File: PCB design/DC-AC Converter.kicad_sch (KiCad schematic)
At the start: 19 parts, among them J1 Screw_Terminal_3.5mm_2, J2 Conn_02x02_Counter_Clockwise, J3 Screw_Terminal_3.5mm_2, J4 Conn_01x02, Q1 IRF9540N, Q2 IRFZ44NSTRLPBF, Q3 IRF9540N, Q4 IRFZ44NSTRLPBF, U1 ATtiny85V-10P, U3 L78L05_SOT89

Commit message: some SMD components changed to PTH footprint
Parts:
- Q1, Q2, Q4: footprint Package_TO_SOT_SMD:TO-263-2 -> Package_TO_SOT_THT:TO-264-3_Horizontal_TabDown
- U1: footprint Package_SO:SOP-8_5.28x5.23mm_P1.27mm -> Package_DIP:DIP-8_W7.62mm_Socket
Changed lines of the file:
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@@
 		)
 		(instances
-			(project "AC_M V2"
+			(project "DC-AC Converter"
 				(path "/907d77e3-c168-455a-b3e6-ab5b57505f53"
 					(reference "FID1")
@@
 		)
 		(instances
-			(project "AC_M V2"
+			(project "DC-AC Converter"
 				(path "/907d77e3-c168-455a-b3e6-ab5b57505f53"
 					(reference "H4")
@@
 		)
 		(instances
-			(project "AC_M V2"
+			(project "DC-AC Converter"
 				(path "/907d77e3-c168-455a-b3e6-ab5b57505f53"
 					(reference "J4")
@@
 		)
 		(instances
-			(project "AC_M V2"
+			(project "DC-AC Converter"
 				(path "/907d77e3-c168-455a-b3e6-ab5b57505f53"
 					(reference "#PWR05")
@@
 			)
 		)
-		(property "Footprint" "Package_TO_SOT_SMD:TO-263-2"
+		(property "Footprint" "Package_TO_SOT_THT:TO-264-3_Horizontal_TabDown"
 			(at 166.37 119.38 0)
 			(effects
@@
 		)
 		(instances
-			(project "AC_M V2"
+			(project "DC-AC Converter"
 				(path "/907d77e3-c168-455a-b3e6-ab5b57505f53"
 					(reference "Q2")
@@
 		)
 		(instances
-			(project "AC_M V2"
+			(project "DC-AC Converter"
 				(path "/907d77e3-c168-455a-b3e6-ab5b57505f53"
 					(reference "#PWR03")
@@
 		)
 		(instances
-			(project "AC_M V2"
+			(project "DC-AC Converter"
 				(path "/907d77e3-c168-455a-b3e6-ab5b57505f53"
 					(reference "H2")
@@
 		)
 		(instances
-			(project "AC_M V2"
+			(project "DC-AC Converter"
 				(path "/907d77e3-c168-455a-b3e6-ab5b57505f53"
 					(reference "J3")
@@
 		)
 		(instances
-			(project "AC_M V2"
+			(project "DC-AC Converter"
 				(path "/907d77e3-c168-455a-b3e6-ab5b57505f53"
 					(reference "D1")
@@
 		)
 		(instances
-			(project "AC_M V2"
+			(project "DC-AC Converter"
 				(path "/907d77e3-c168-455a-b3e6-ab5b57505f53"
 					(reference "#PWR04")
@@
 		)
 		(instances
-			(project "AC_M V2"
+			(project "DC-AC Converter"
 				(path "/907d77e3-c168-455a-b3e6-ab5b57505f53"
 					(reference "#PWR02")
@@
 		)
 		(instances
-			(project "AC_M V2"
+			(project "DC-AC Converter"
 				(path "/907d77e3-c168-455a-b3e6-ab5b57505f53"
 					(reference "U3")
@@
 		)
 		(instances
-			(project "AC_M V2"
+			(project "DC-AC Converter"
 				(path "/907d77e3-c168-455a-b3e6-ab5b57505f53"
 					(reference "J2")
@@
 		)
 		(instances
-			(project "AC_M V2"
+			(project "DC-AC Converter"
 				(path "/907d77e3-c168-455a-b3e6-ab5b57505f53"
 					(reference "#PWR01")
@@
 			)
 		)
-		(property "Datasheet" "http://www.irf.com/product-info/datasheets/data/irf9540n.pdf"
+		(property "Datasheet" "Package_TO_SOT_THT:TO-264-3_Horizontal_TabDown"
 			(at 213.36 52.07 0)
 			(effects
@@
 		)
 		(instances
-			(project "AC_M V2"
+			(project "DC-AC Converter"
 				(path "/907d77e3-c168-455a-b3e6-ab5b57505f53"
 					(reference "Q3")
@@
 		)
 		(instances
-			(project "AC_M V2"
+			(project "DC-AC Converter"
 				(path "/907d77e3-c168-455a-b3e6-ab5b57505f53"
 					(reference "#PWR06")
@@
 			)
 		)
-		(property "Footprint" "Package_TO_SOT_SMD:TO-263-2"
+		(property "Footprint" "Package_TO_SOT_THT:TO-264-3_Horizontal_TabDown"
 			(at 213.36 121.92 0)
 			(effects
@@
 		)
 		(instances
-			(project "AC_M V2"
+			(project "DC-AC Converter"
 				(path "/907d77e3-c168-455a-b3e6-ab5b57505f53"
 					(reference "Q4")
@@
 		)
 		(instances
-			(project "AC_M V2"
+			(project "DC-AC Converter"
 				(path "/907d77e3-c168-455a-b3e6-ab5b57505f53"
 					(reference "C1")
@@
 			)
 		)
-		(property "Footprint" "Package_TO_SOT_SMD:TO-263-2"
+		(property "Footprint" "Package_TO_SOT_THT:TO-264-3_Horizontal_TabDown"
 			(at 166.37 51.435 0)
 			(effects
@@
 		)
 		(instances
-			(project "AC_M V2"
+			(project "DC-AC Converter"
 				(path "/907d77e3-c168-455a-b3e6-ab5b57505f53"
 					(reference "Q1")
@@
 		)
 		(instances
-			(project "AC_M V2"
+			(project "DC-AC Converter"
 				(path "/907d77e3-c168-455a-b3e6-ab5b57505f53"
 					(reference "FID2")
@@
 			)
 		)
-		(property "Footprint" "Package_SO:SOP-8_5.28x5.23mm_P1.27mm"
+		(property "Footprint" "Package_DIP:DIP-8_W7.62mm_Socket"
 			(at 121.92 73.66 0)
 			(effects
@@
 		)
 		(instances
-			(project "AC_M V2"
+			(project "DC-AC Converter"
 				(path "/907d77e3-c168-455a-b3e6-ab5b57505f53"
 					(reference "U1")
@@
 		)
 		(instances
-			(project "AC_M V2"
+			(project "DC-AC Converter"
 				(path "/907d77e3-c168-455a-b3e6-ab5b57505f53"
 					(reference "J1")
@@
 		)
 		(instances
-			(project "AC_M V2"
+			(project "DC-AC Converter"
 				(path "/907d77e3-c168-455a-b3e6-ab5b57505f53"
 					(reference "R1")
@@
 		)
 		(instances
-			(project "AC_M V2"
+			(project "DC-AC Converter"
 				(path "/907d77e3-c168-455a-b3e6-ab5b57505f53"
 					(reference "H1")
@@
 		)
 		(instances
-			(project "AC_M V2"
+			(project "DC-AC Converter"
 				(path "/907d77e3-c168-455a-b3e6-ab5b57505f53"
 					(reference "H3")

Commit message: PCB/Board added
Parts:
- removed FID1, FID2: Fiducial, Fiducial:Fiducial_0.5mm_Mask1mm, symbol Mechanical:Fiducial
- removed H1, H2: MountingHole_Pad, MountingHole:MountingHole_2.2mm_M2_DIN965_Pad, symbol Mechanical:MountingHole_Pad
- removed H3, H4: MountingHole, MountingHole:MountingHole_3.2mm_M3, symbol Mechanical:MountingHole
- C1: footprint Capacitor_SMD:CP_Elec_4x5.3 -> Capacitor_THT:CP_Radial_D5.0mm_P2.00mm
- D1: footprint LED_SMD:LED_1206_3216Metric_Pad1.42x1.75mm_HandSolder -> LED_THT:LED_D5.0mm
- Q3: footprint Package_TO_SOT_SMD:TO-263-2 -> Package_TO_SOT_THT:TO-264-3_Horizontal_TabDown
- Q4: footprint Package_TO_SOT_THT:TO-264-3_Horizontal_TabDown -> IRFZ44NSTRLPBF:DPAK254P1524X483-3N
- R1: footprint Resistor_SMD:R_1206_3216Metric -> Resistor_THT:R_Axial_DIN0204_L3.6mm_D1.6mm_P5.08mm_Horizontal

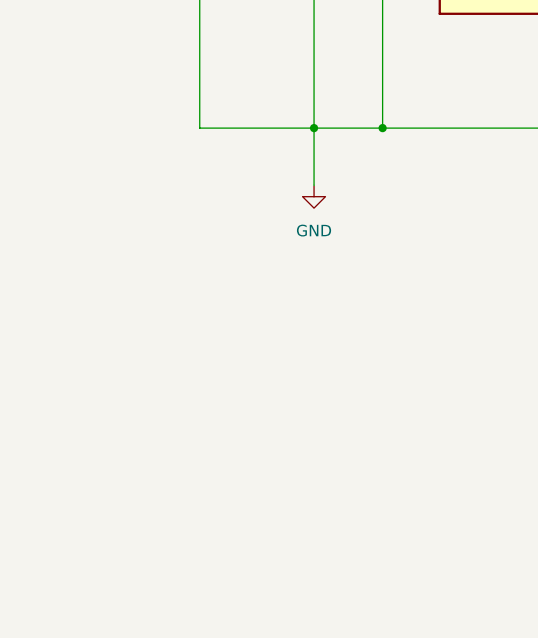
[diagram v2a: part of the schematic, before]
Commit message: Improved silk screen and branded the PCB with FundiBots logo
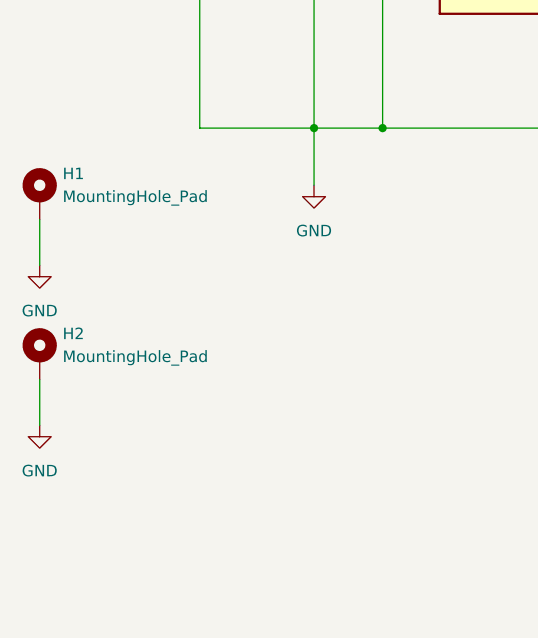
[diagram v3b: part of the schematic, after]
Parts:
- added H1, H2: MountingHole_Pad, MountingHole:MountingHole_2.2mm_M2_DIN965_Pad_TopBottom, symbol Mechanical:MountingHole_Pad
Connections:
- net GND: now also H1.1, H2.1

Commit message: Improved on PCB
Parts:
- R1: value R -> 330
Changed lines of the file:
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@@
 			)
 		)
-		(property "Value" "R"
+		(property "Value" "330"
 			(at 105.41 58.42 0)
 			(effects
